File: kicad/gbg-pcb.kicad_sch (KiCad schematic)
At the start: 53 parts, among them IC1 AP74700QW6-7, IC2 D78B05T-1.0, J1 9 2.54mm pitch header pins, J2 Conn_01x02, J3 VP0265840000G, J4 Screw_Terminal_01x04, J5 Screw_Terminal_01x03, J6 screw terminal, J7 2 2.54mm pitch header pins, J8 1017514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

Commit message: change and label capacitors
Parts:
- C4, C6, C7, C8: value 22 uF -> 220nF; Manufacturer_Part_Number CL31A226KAHNNNE -> CL31B224KBFNNNE; digikey_part_number 1276-3047-1-ND -> 1276-1106-1-ND; price 0.1 -> 0.03
- renumbered TP4 to TP3, TP3 to TP4, U2 to U1, U1 to U2
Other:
- note added: "PSMN1R2-25YLDX 0.0015Ohm, 50 K/W, sqrt(2W/rds)=36A I put two mosfets in parallel"
- note added: "SR to ground gives fastest switching time it is the most efficient (and easiest to wire), but could make more electrical noise"
- note removed: "3 pins or just 2 pins?"
- note removed: "PSMN1R2-25YLDX 0.0015Ohm, 50 K/W, sqrt(2W/rds)=36A I put two mosfets in parallel. is that ok? can IC1 handle that?"
- note removed: "SR to ground gives fastest switching time it is the most efficient (and easiest to wire), but could make more electrical noise Maybe it would also increase voltage spikes from inductors in motors so maybe review this?"
- note removed: "add fuse? https://www.digikey.com/en/products/detail/optifuse/ACB2-PL-35A/11578424"
- note removed: "check continuous current of the half bridges - I'm worried about thermal limits"
- note removed: "check continuous current of the mosfets - I'm worried about thermal limits"
- note removed: "ok to leave disconnected?"
- note removed: "power switch"
- moved on the sheet: TP4

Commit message: update values for bom
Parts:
- HS1, HS2, HS3: mount_type tht -> Do Not Place
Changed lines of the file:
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@@
 			)
 		)
-		(property "mount_type" "tht"
+		(property "mount_type" "Do Not Place"
 			(at 44.45 234.95 0)
 			(effects
@@
 			)
 		)
-		(property "mount_type" "tht"
+		(property "mount_type" "Do Not Place"
 			(at 35.56 245.11 0)
 			(effects
@@
 			)
 		)
-		(property "mount_type" "tht"
+		(property "mount_type" "Do Not Place"
 			(at 52.07 245.11 0)
 			(effects

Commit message: fix mosfet circuit
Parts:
- removed C1, C2: 220nF, Capacitor_SMD:C_1206_3216Metric_Pad1.33x1.80mm_HandSolder, symbol Device:C
- removed IC1: AP74700QW6-7, Package_TO_SOT_SMD:SOT-23-6_Handsoldering, symbol library:AP74700QW6-7
- removed J7: 2 2.54mm pitch header pins, Connector_PinHeader_2.54mm:PinHeader_1x02_P2.54mm_Vertical, symbol Connector:Conn_01x02_Pin
- added Q3, Q4: PSMN1R2-25YLDX, Package_TO_SOT_SMD:LFPAK56, symbol Simulation_SPICE:NMOS
- added R5: 2.2k, Resistor_SMD:R_1206_3216Metric_Pad1.30x1.75mm_HandSolder, symbol Device:R
- added R7: 680, Resistor_SMD:R_1206_3216Metric_Pad1.30x1.75mm_HandSolder, symbol Device:R
- renumbered J6 to J12
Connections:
- net +BATT: now also J1.12 (Pin_12), J12.2 (Pin_2), J3.3, J3.4, Q1.4 (G), Q2.4 (G), SW1.1 (A); no longer J12.1 (Pin_1), Q1.5 (D), Q2.5 (D)
- net GND: now also J12.1 (Pin_1), Q3.5 (D), Q4.5 (D); no longer J1.12 (Pin_12), J12.2 (Pin_2), J3.1, J3.2
- net at SW1.2 (B): now also R7.1
- net at Q1.1 (S), Q1.2 (S), Q1.3 (S)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: now also Q3.1 (S), Q3.2 (S), Q3.3 (S), Q4.1 (S), Q4.2 (S), Q4.3 (S), R5.2; no longer J3.3, J3.4, SW1.1 (A)
- new net: J3.1, J3.2, Q1.5 (D), Q2.5 (D)
- new net: Q3.4 (G), Q4.4 (G), R5.1, R7.2
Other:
- note added: "NMOS"
- note added: "on/off switch"
- note added: "reverse polarity protection"
- note removed: "PSMN1R2-25YLDX 0.0015Ohm, 50 K/W, sqrt(2W/rds)=36A I put two mosfets in parallel"
- moved on the sheet: 3V1, 5V1, C10, C9, IC2, J12, J2, J3, Q1, R2, R3, R4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

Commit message: v1.1
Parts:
- C3, C5: footprint Capacitor_THT:CP_Radial_D10.0mm_P7.50mm -> kicad libraries:CP_Radial_D10.0mm_P5.00mm
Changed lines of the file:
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@@
 			)
 		)
-		(property "Footprint" "Capacitor_THT:CP_Radial_D10.0mm_P7.50mm"
+		(property "Footprint" "kicad libraries:CP_Radial_D10.0mm_P5.00mm"
 			(at 216.8652 120.65 0)
 			(effects
@@
 			)
 		)
-		(property "Footprint" "Capacitor_THT:CP_Radial_D10.0mm_P7.50mm"
+		(property "Footprint" "kicad libraries:CP_Radial_D10.0mm_P5.00mm"
 			(at 204.1652 38.1 0)
 			(effects

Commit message: adjust labels
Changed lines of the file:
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@@
 		(dnp no)
 		(property "Reference" "Q2"
-			(at 150.622 242.316 90)
+			(at 150.876 242.316 90)
 			(effects
 				(font

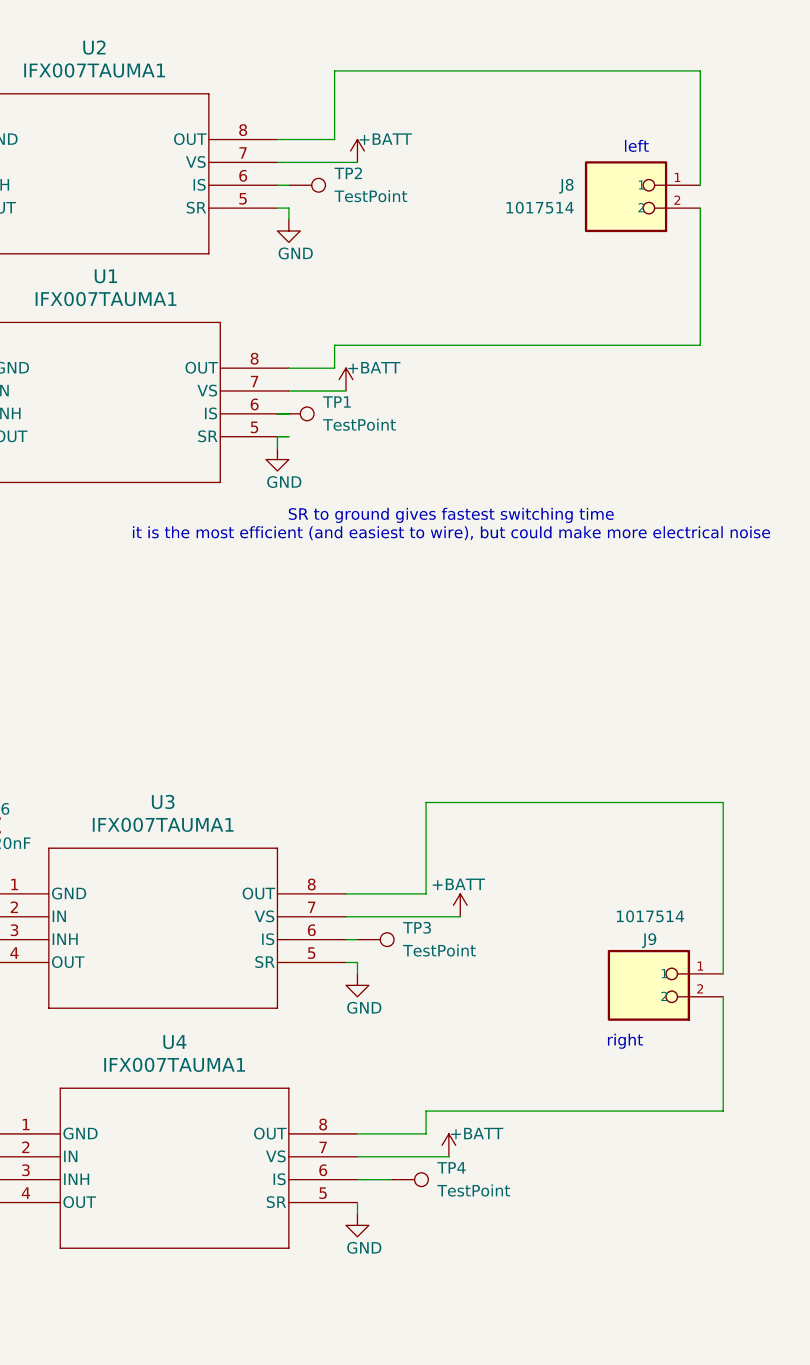
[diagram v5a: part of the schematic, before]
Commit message: adjust layout and heatsink
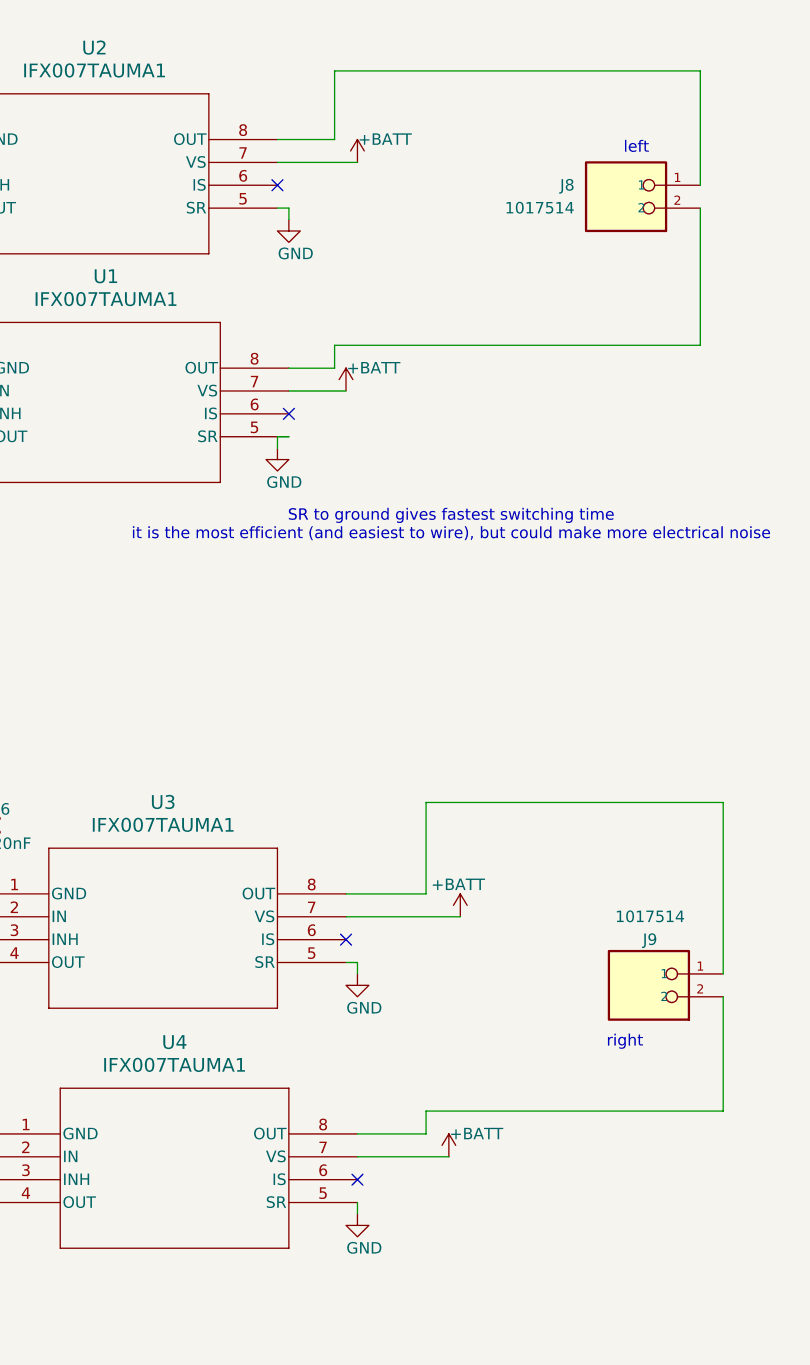
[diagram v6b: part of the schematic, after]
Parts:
- removed TP1, TP2, TP3, TP4: TestPoint, TestPoint:TestPoint_Pad_D1.0mm, symbol Connector:TestPoint
- HS1: footprint kicad libraries:SK 675 100 AL -> kicad libraries:SK 582 100 AL; Manufacturer_Part_Number SK 675 100 AL -> SK 582 100 AL; digikey_part_number 5496-SK675100AL-ND -> 5496-SK582100AL-ND; mount_type Do Not Place -> DNP for PCB assembly; price 1.32 -> 1
- HS2, HS3: Manufacturer_Part_Number TG-T1000-42-18-0.25-5PT -> TG-T1000-43-20-0.25-5PT; digikey_part_number 1168-TG-T1000-42-18-0.25-5PT-ND -> 1168-TG-T1000-43-20-0.25-5PT-ND; mount_type Do Not Place -> white side on pcb; price 0.303 -> .31
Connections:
- no-connect marks 8 -> 12

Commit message: adjust layout
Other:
- note removed: "SR to ground gives fastest switching time it is the most efficient (and easiest to wire), but could make more electrical noise"
- moved on the sheet: C5, C6, C8, J9, U3, U4

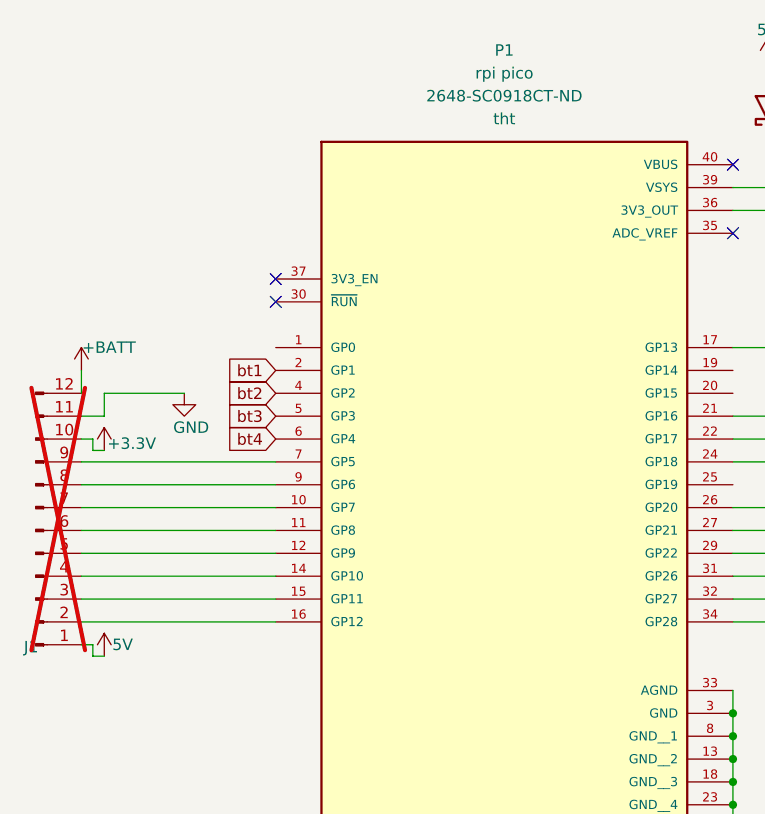
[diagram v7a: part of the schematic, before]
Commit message: v1.2 (update BOM and adjust silkscreen)
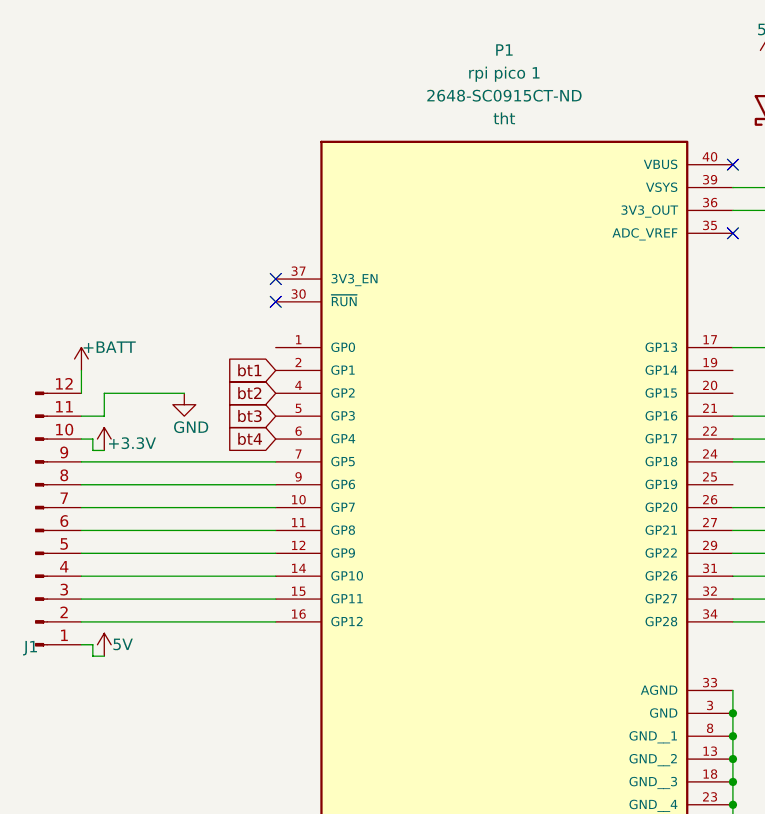
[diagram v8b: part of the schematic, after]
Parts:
- HS1: mount_type DNP for PCB assembly -> tht, use HS2 and HS3 to attach, buy in multiples of 10
- HS2, HS3: mount_type white side on pcb -> tht
- J1: value 9 2.54mm pitch header pins -> 12 2.54mm pitch header pins; Manufacturer_Name (none) -> Any Manufacturer; Manufacturer_Part_Number (none) -> PH1-12-UA; digikey_part_number (none) -> 2057-PH1-12-UA-ND; price (none) -> 0.16; now fitted; now in the parts list
- P1: value rpi pico -> rpi pico 1; Manufacturer_Part_Number SC0918 -> SC0915; digikey_part_number 2648-SC0918CT-ND -> 2648-SC0915CT-ND; price 6.0 -> 4.00
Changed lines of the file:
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@@
 			)
 		)
-		(property "mount_type" "DNP for PCB assembly"
+		(property "mount_type" "tht, use HS2 and HS3 to attach, buy in multiples of 10"
 			(at 44.45 234.95 0)
 			(effects
@@
 		(unit 1)
 		(exclude_from_sim no)
-		(in_bom no)
+		(in_bom yes)
 		(on_board yes)
-		(dnp yes)
+		(dnp no)
 		(property "Reference" "J1"
 			(at 21.082 89.154 0)
@@
 			)
 		)
-		(property "Value" "9   2.54mm pitch header pins"
+		(property "Value" "12  2.54mm pitch header pins"
 			(at 16.256 65.786 0)
 			(effects
@@
 			)
 		)
-		(property "Datasheet" "~"
+		(property "Datasheet" "https://www.digikey.com/en/products/detail/adam-tech/PH1-12-UA/9830395"
 			(at 21.59 76.2 0)
 			(effects
@@
 			)
 		)
-		(property "Manufacturer_Name" ""
+		(property "Manufacturer_Name" "Any Manufacturer"
 			(at 21.59 76.2 0)
 			(effects
@@
 			)
 		)
-		(property "Manufacturer_Part_Number" ""
+		(property "Manufacturer_Part_Number" "PH1-12-UA"
 			(at 21.59 76.2 0)
 			(effects
@@
 			)
 		)
-		(property "price" ""
+		(property "price" "0.16"
 			(at 21.59 76.2 0)
 			(effects
@@
 			)
 		)
-		(property "digikey_part_number" ""
+		(property "digikey_part_number" "2057-PH1-12-UA-ND"
 			(at 21.59 76.2 0)
 			(effects
@@
 			)
 		)
-		(property "mount_type" "white side on pcb"
+		(property "mount_type" "tht"
 			(at 35.56 245.11 0)
 			(effects
@@
 			)
 		)
-		(property "Value" "rpi pico"
+		(property "Value" "rpi pico 1"
 			(at 73.66 25.4 0)
 			(effects
@@
 			)
 		)
-		(property "Datasheet" "https://www.digikey.com/en/products/detail/raspberry-pi/SC0918/16608263"
+		(property "Datasheet" "https://www.digikey.com/en/products/detail/raspberry-pi/SC0915/13624793"
 			(at 73.66 76.2 0)
 			(effects
@@
 			)
 		)
-		(property "price" "6.0"
+		(property "price" "4.00"
 			(at 73.66 76.2 0)
 			(effects
@@
 			)
 		)
-		(property "Manufacturer_Part_Number" "SC0918"
+		(property "Manufacturer_Part_Number" "SC0915"
 			(at 73.66 76.2 0)
 			(effects
@@
 			)
 		)
-		(property "digikey_part_number" "2648-SC0918CT-ND"
+		(property "digikey_part_number" "2648-SC0915CT-ND"
 			(at 73.66 27.94 0)
 			(effects
@@
 			)
 		)
-		(property "mount_type" "white side on pcb"
+		(property "mount_type" "tht"
 			(at 52.07 245.11 0)
 			(effects
